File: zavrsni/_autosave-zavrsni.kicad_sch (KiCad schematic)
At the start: 62 parts, among them Q1 BC337, Q2 BC317, SW1 RotaryEncoder_Switch, SW2 SW_Push, SW3 SW_Push, SW4 SW_Push, SW5 SW_Push, SW6 SW_Push, SW7 SW_Push, SW8 SW_Push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

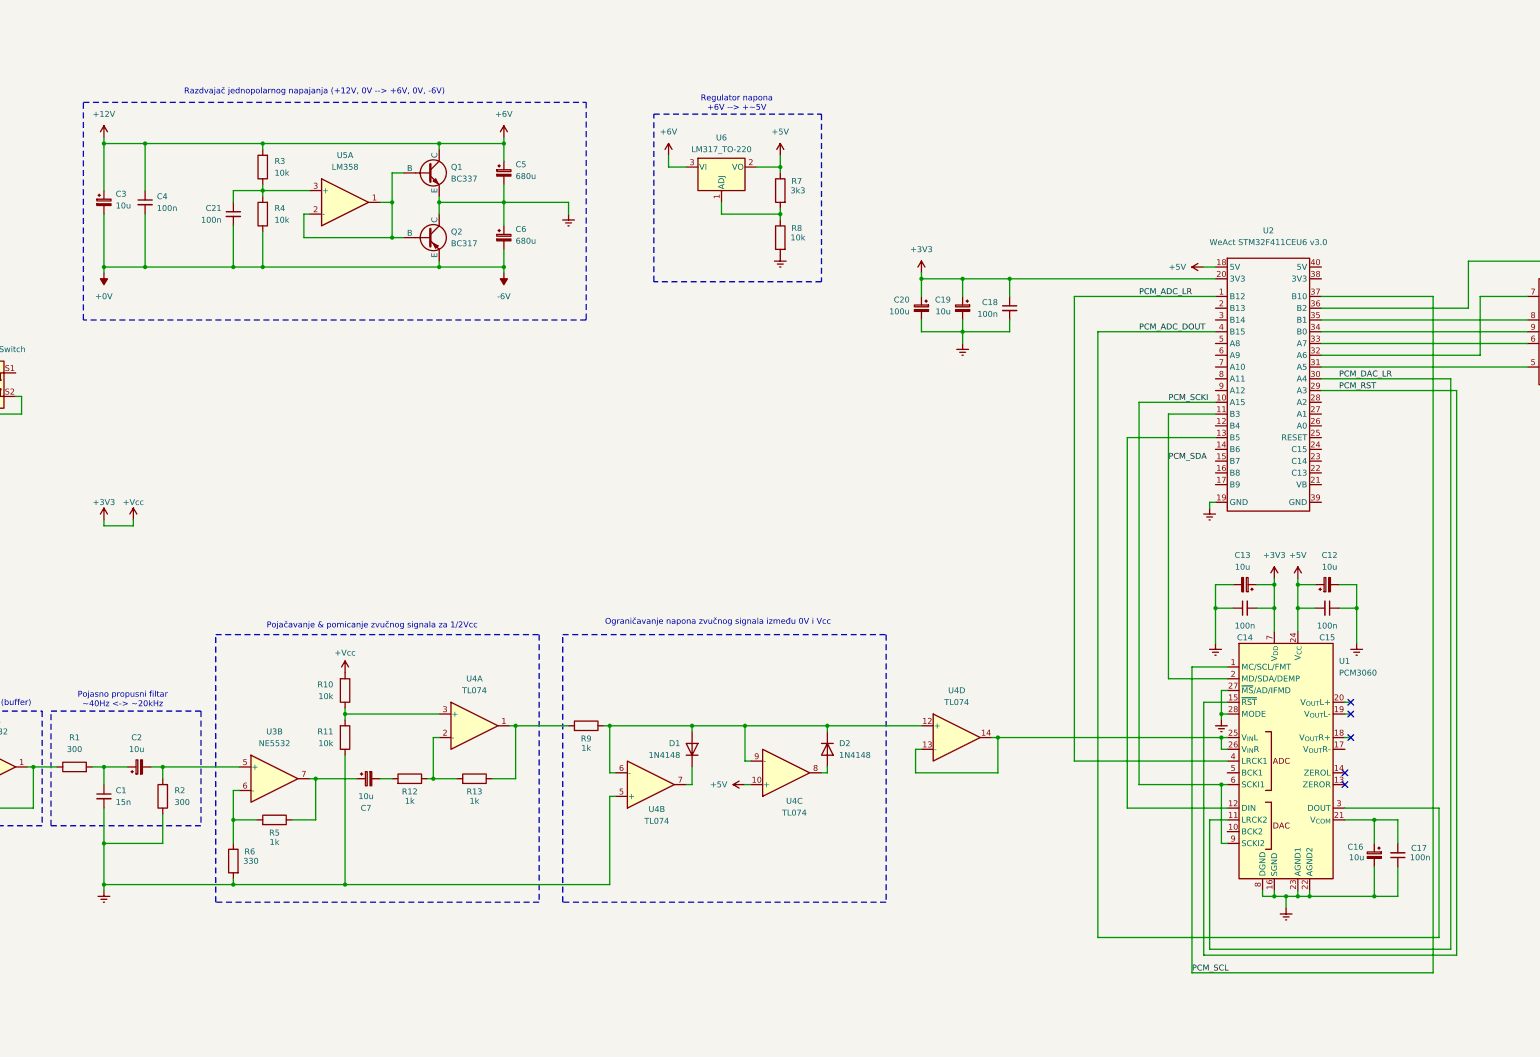
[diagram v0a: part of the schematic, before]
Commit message: ima errore PCM3060 -> STM32 ADC & CS4335 (PS2)
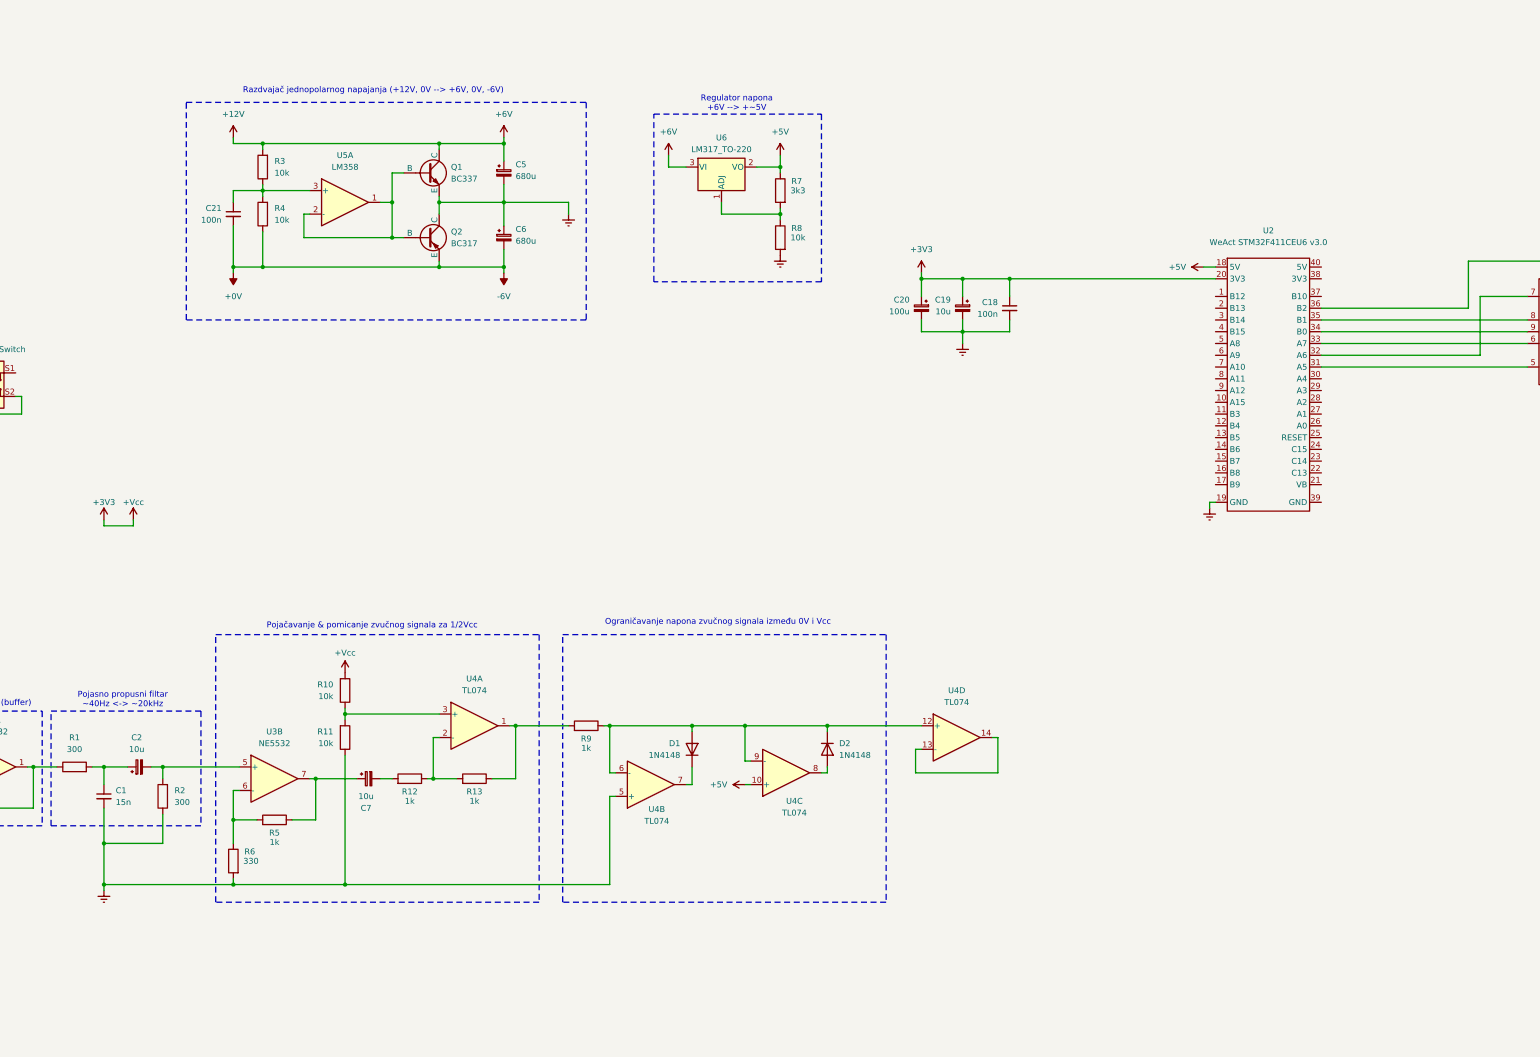
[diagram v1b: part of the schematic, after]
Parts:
- removed C12, C13, C16, C3: 10u, Capacitor_THT:CP_Radial_D5.0mm_P2.50mm, symbol Device:C_Polarized_Small
- removed C14, C15, C17, C4: 100n, Capacitor_THT:C_Disc_D5.0mm_W2.5mm_P5.00mm, symbol Device:C_Small
- removed U1: PCM3060, Package_DIP:DIP-28_W15.24mm_Socket, symbol Audio:PCM3060
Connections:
- net PCM_ADC_DOUT: no longer names the net of U2.4 (B15)
- net PCM_ADC_LR: no longer names the net of U2.1 (B12)
- net PCM_DAC_LR: no longer names the net of U2.30 (A4)
- net PCM_RST: no longer names the net of U2.29 (A3)
- net PCM_SCKI: no longer names the net of U2.10 (A15)
- net PCM_SCL: no longer names the net of U2.37 (B10)
- net PCM_SDA: no longer names the net of U2.11 (B3)
- no-connect marks 5 -> 0
